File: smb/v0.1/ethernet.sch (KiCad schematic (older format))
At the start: 22 parts, among them J401 HR911105_RJ45, U201 ENC28J60, U301 74HC08, X201 25MHz

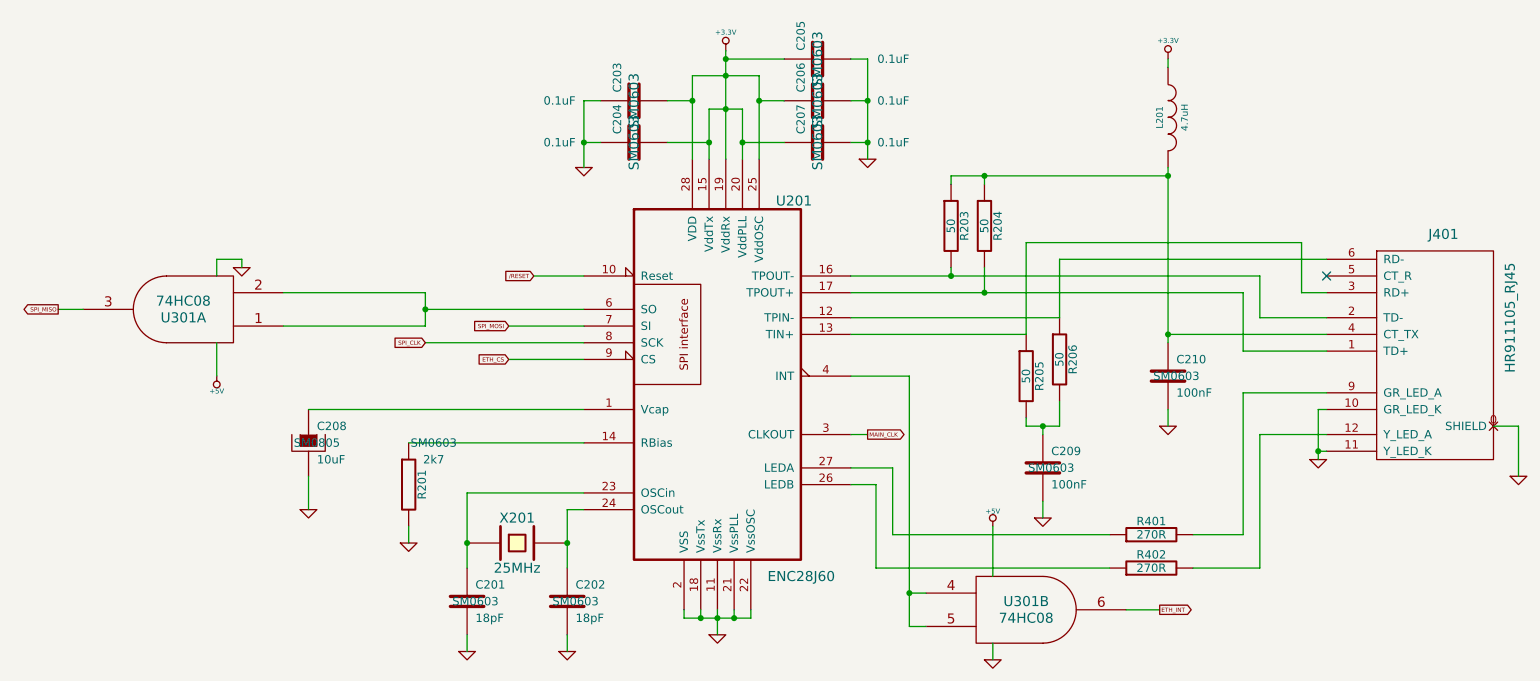
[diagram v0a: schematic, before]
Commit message: correction broche 8 du module RS485 + inversion tx+/tx- au niveau du connecteur + pilotage E/R independant inversion polarit? connecteur d'alim d?placement slot pour rtc simplification routage et optimisation plan de masse (affinage zone exclusion)
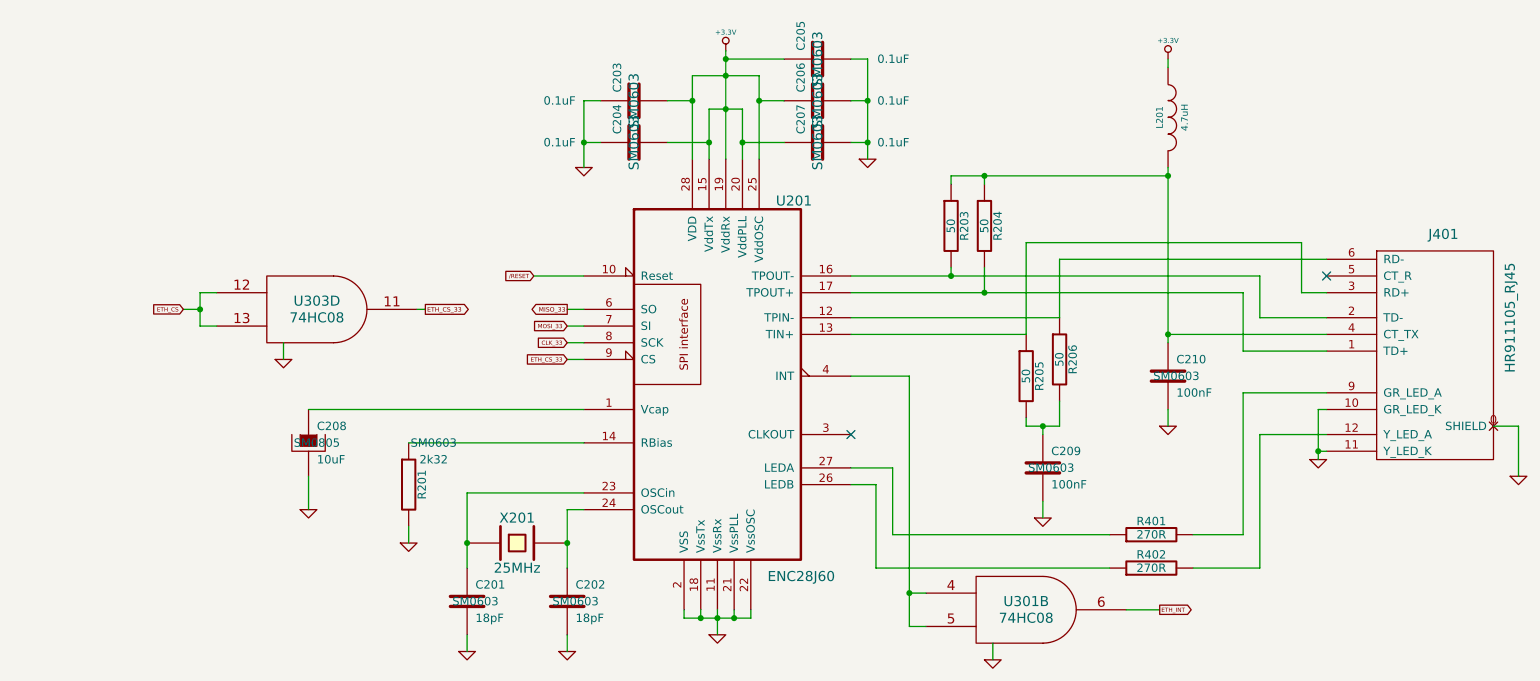
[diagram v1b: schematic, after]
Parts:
- R201: value 2k7 -> 2k32
- renumbered U301 to U303
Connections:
- net ETH_CS: now also U303.12, U303.13; no longer U201.9 (CS)
- net +5V: no longer names the net of U303.14 (VCC)
- net +5V: no longer U301.14 (VCC)
- net MAIN_CLK: no longer names the net of U201.3 (CLKOUT)
- net SPI_CLK renamed CLK_33
- removed net SPI_MISO: U303.3
- net SPI_MOSI renamed MOSI_33
- new net ETH_CS_33: U201.9 (CS), U303.11
- new net MISO_33: U201.6 (SO)
- no-connect marks 1 -> 2
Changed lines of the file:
@@
-EESchema Schematic File Version 2  date jeu. 23 mai 2013 13:21:39 CEST
+EESchema Schematic File Version 2  date mar. 28 mai 2013 22:08:00 CEST
 LIBS:power
 LIBS:device
@@
 LIBS:dual_self
 LIBS:ALPS_SWITCHS
+LIBS:max485
 LIBS:SMB-cache
-EELAYER 27 0
+EELAYER 24 0
 EELAYER END
 $Descr A4 11693 8268
@@
 Sheet 4 4
 Title "Short Main Board - SMB controler"
-Date "23 may 2013"
+Date "28 may 2013"
 Rev "0"
 Comp "XPLDUINO project"
@@
 Wire Wire Line
 	8700 4350 9000 4350
-Wire Wire Line
-	7500 5000 7500 5100
-Wire Wire Line
-	2850 3200 2850 3400
 Connection ~ 7000 4700
 Wire Wire Line
 	7100 4700 7000 4700
-Wire Wire Line
-	2050 3000 1900 3000
-Wire Wire Line
-	3250 2900 4100 2900
 Connection ~ 7450 2200
 Wire Wire Line
@@
 	4750 2800 5050 2800
 Wire Wire Line
-	6650 3750 6750 3750
-Wire Wire Line
-	4600 3100 5050 3100
-Wire Wire Line
-	4100 3200 5050 3200
-Wire Wire Line
 	4000 3800 5050 3800
 Wire Wire Line
@@
 	3400 3600 5050 3600
 Wire Wire Line
-	4100 3000 5050 3000
-Wire Wire Line
-	4600 3300 5050 3300
-Wire Wire Line
 	6650 3050 7900 3050
 Wire Wire Line
@@
 Connection ~ 8550 2200
 Wire Wire Line
-	4100 2900 4100 3100
-Wire Wire Line
-	4100 3100 3250 3100
-Connection ~ 4100 3000
-Wire Wire Line
 	6650 3400 7000 3400
 Wire Wire Line
@@
 Wire Wire Line
 	8300 4800 8500 4800
-Wire Wire Line
-	2850 2800 2850 2700
-Wire Wire Line
-	2850 2700 3000 2700
-Wire Wire Line
-	3000 2700 3000 2750
-Wire Wire Line
-	7500 4300 7500 4600
 Wire Wire Line
 	6900 4350 8200 4350
@@
 $EndComp
 $Comp
-L +5V #PWR086
-U 1 1 4FDE1BE4
-P 7500 4300
-F 0 "#PWR086" H 7500 4390 20  0001 C CNN
-F 1 "+5V" H 7500 4390 30  0000 C CNN
-F 2 "" H 7500 4300 60  0001 C CNN
-F 3 "" H 7500 4300 60  0001 C CNN
-	1    7500 4300
-	1    0    0    -1
-$EndComp
-$Comp
-L GND #PWR087
-U 1 1 4FDE1B8D
-P 7500 5100
-F 0 "#PWR087" H 7500 5100 30  0001 C CNN
-F 1 "GND" H 7500 5030 30  0001 C CNN
-F 2 "" H 7500 5100 60  0001 C CNN
-F 3 "" H 7500 5100 60  0001 C CNN
-	1    7500 5100
-	1    0    0    -1
-$EndComp
-$Comp
-L GND #PWR088
-U 1 1 4FDE1B70
-P 3000 2750
-F 0 "#PWR088" H 3000 2750 30  0001 C CNN
-F 1 "GND" H 3000 2680 30  0001 C CNN
-F 2 "" H 3000 2750 60  0001 C CNN
-F 3 "" H 3000 2750 60  0001 C CNN
-	1    3000 2750
-	1    0    0    -1
-$EndComp
-$Comp
-L +5V #PWR089
-U 1 1 4FDE1B61
-P 2850 3400
-F 0 "#PWR089" H 2850 3490 20  0001 C CNN
-F 1 "+5V" H 2850 3490 30  0000 C CNN
-F 2 "" H 2850 3400 60  0001 C CNN
-F 3 "" H 2850 3400 60  0001 C CNN
-	1    2850 3400
-	-1   0    0    1
-$EndComp
-$Comp
 L 74HC08 U301
 U 2 1 4FDE1879
@@
 $EndComp
 $Comp
-L 74HC08 U301
-U 1 1 4FDE1808
-P 2650 3000
-F 0 "U301" H 2650 3050 60  0000 C CNN
-F 1 "74HC08" H 2650 2950 60  0000 C CNN
-F 2 "" H 2650 3000 60  0001 C CNN
-F 3 "" H 2650 3000 60  0001 C CNN
-	1    2650 3000
-	-1   0    0    1
-$EndComp
-$Comp
 L R R204
 U 1 1 4FA00FEC
@@
 $EndComp
 $Comp
-L +3.3V #PWR090
+L +3.3V #PWR083
 U 1 1 4FA00F89
 P 8550 1500
-F 0 "#PWR090" H 8550 1460 30  0001 C CNN
+F 0 "#PWR083" H 8550 1460 30  0001 C CNN
 F 1 "+3.3V" H 8550 1610 30  0000 C CNN
 F 2 "" H 8550 1500 60  0001 C CNN
@@
 $EndComp
 $Comp
-L GND #PWR091
+L GND #PWR084
 U 1 1 4FA00F53
 P 8550 3700
-F 0 "#PWR091" H 8550 3700 30  0001 C CNN
+F 0 "#PWR084" H 8550 3700 30  0001 C CNN
 F 1 "GND" H 8550 3630 30  0001 C CNN
 F 2 "" H 8550 3700 60  0001 C CNN
@@
 $EndComp
 $Comp
-L GND #PWR092
+L GND #PWR085
 U 1 1 4FA00C7B
 P 9450 3900
-F 0 "#PWR092" H 9450 3900 30  0001 C CNN
+F 0 "#PWR085" H 9450 3900 30  0001 C CNN
 F 1 "GND" H 9450 3830 30  0001 C CNN
 F 2 "" H 9450 3900 60  0001 C CNN
@@
 $EndComp
 $Comp
-L GND #PWR093
+L GND #PWR086
 U 1 1 4FA00C63
 P 10650 4000
-F 0 "#PWR093" H 10650 4000 30  0001 C CNN
+F 0 "#PWR086" H 10650 4000 30  0001 C CNN
 F 1 "GND" H 10650 3930 30  0001 C CNN
 F 2 "" H 10650 4000 60  0001 C CNN
@@
 $EndComp
 $Comp
-L GND #PWR094
+L GND #PWR087
 U 1 1 4F9FF676
 P 7800 4250
-F 0 "#PWR094" H 7800 4250 30  0001 C CNN
+F 0 "#PWR087" H 7800 4250 30  0001 C CNN
 F 1 "GND" H 7800 4180 30  0001 C CNN
 F 2 "" H 7800 4250 60  0001 C CNN
@@
 Text GLabel 8500 4800 2    25   Output ~ 0
 ETH_INT
-Text GLabel 6750 3750 2    25   Output ~ 0
-MAIN_CLK
-Text GLabel 1900 3000 0    25   Output ~ 0
-SPI_MISO
-Text GLabel 4600 3100 0    25   Input ~ 0
-SPI_MOSI
-Text GLabel 4600 3300 0    25   Input ~ 0
-ETH_CS
-Text GLabel 4100 3200 0    25   Input ~ 0
-SPI_CLK
-$Comp
-L GND #PWR095
+Text GLabel 4950 3100 0    25   Input ~ 0
+MOSI_33
+Text GLabel 4950 3300 0    25   Input ~ 0
+ETH_CS_33
+Text GLabel 4950 3200 0    25   Input ~ 0
+CLK_33
+$Comp
+L GND #PWR088
 U 1 1 4F9FEE21
 P 3400 4200
-F 0 "#PWR095" H 3400 4200 30  0001 C CNN
+F 0 "#PWR088" H 3400 4200 30  0001 C CNN
 F 1 "GND" H 3400 4130 30  0001 C CNN
 F 2 "" H 3400 4200 60  0001 C CNN
@@
 $EndComp
 $Comp
-L GND #PWR096
+L GND #PWR089
 U 1 1 4F9FEE1E
 P 4000 4400
-F 0 "#PWR096" H 4000 4400 30  0001 C CNN
+F 0 "#PWR089" H 4000 4400 30  0001 C CNN
 F 1 "GND" H 4000 4330 30  0001 C CNN
 F 2 "" H 4000 4400 60  0001 C CNN
@@
 P 4000 4050
 F 0 "R201" V 4080 4050 50  0000 C CNN
-F 1 "2k7" H 4150 4200 50  0000 C CNN
+F 1 "2k32" H 4150 4200 50  0000 C CNN
 F 2 "SM0603" H 4150 4300 50  0000 C CNN
 F 3 "" H 4000 4050 60  0001 C CNN
@@
 $EndComp
 $Comp
-L GND #PWR097
+L GND #PWR090
 U 1 1 4F9FC462
 P 5050 2150
-F 0 "#PWR097" H 5050 2150 30  0001 C CNN
+F 0 "#PWR090" H 5050 2150 30  0001 C CNN
 F 1 "GND" H 5050 2080 30  0001 C CNN
 F 2 "" H 5050 2150 60  0001 C CNN
@@
 $EndComp
 $Comp
-L GND #PWR098
+L GND #PWR091
 U 1 1 4F9FC45C
 P 6750 2100
-F 0 "#PWR098" H 6750 2100 30  0001 C CNN
+F 0 "#PWR091" H 6750 2100 30  0001 C CNN
 F 1 "GND" H 6750 2030 30  0001 C CNN
 F 2 "" H 6750 2100 60  0001 C CNN
@@
 $EndComp
 $Comp
-L +3.3V #PWR099
+L +3.3V #PWR092
 U 1 1 4F9FC2EE
 P 5900 1450
-F 0 "#PWR099" H 5900 1410 30  0001 C CNN
+F 0 "#PWR092" H 5900 1410 30  0001 C CNN
 F 1 "+3.3V" H 5900 1560 30  0000 C CNN
 F 2 "" H 5900 1450 60  0001 C CNN
@@
 $EndComp
 $Comp
-L GND #PWR0100
+L GND #PWR093
 U 1 1 4F9D7261
 P 4350 5050
-F 0 "#PWR0100" H 4350 5050 30  0001 C CNN
+F 0 "#PWR093" H 4350 5050 30  0001 C CNN
 F 1 "GND" H 4350 4980 30  0001 C CNN
 F 2 "" H 4350 5050 60  0001 C CNN
@@
 $EndComp
 $Comp
-L GND #PWR0101
+L GND #PWR094
 U 1 1 4F9D725B
 P 4950 5050
-F 0 "#PWR0101" H 4950 5050 30  0001 C CNN
+F 0 "#PWR094" H 4950 5050 30  0001 C CNN
 F 1 "GND" H 4950 4980 30  0001 C CNN
 F 2 "" H 4950 5050 60  0001 C CNN
@@
 $EndComp
 $Comp
-L GND #PWR0102
+L GND #PWR095
 U 1 1 4F9D6E29
 P 5850 4950
-F 0 "#PWR0102" H 5850 4950 30  0001 C CNN
+F 0 "#PWR095" H 5850 4950 30  0001 C CNN
 F 1 "GND" H 5850 4880 30  0001 C CNN
 F 2 "" H 5850 4950 60  0001 C CNN
@@
 $EndComp
 NoConn ~ 9500 2800
+Text GLabel 4950 3000 0    27   Output ~ 0
+MISO_33
+Wire Wire Line
+	4950 3000 5050 3000
+Wire Wire Line
+	4950 3100 5050 3100
+Wire Wire Line
+	4950 3200 5050 3200
+Wire Wire Line
+	4950 3300 5050 3300
+Text GLabel 4100 3000 2    27   Output ~ 0
+ETH_CS_33
+Wire Wire Line
+	4050 3000 4100 3000
+Text GLabel 2650 3000 0    25   Input ~ 0
+ETH_CS
+Wire Wire Line
+	2650 3000 2750 3000
+Wire Wire Line
+	2750 2900 2750 3100
+Wire Wire Line
+	2750 2900 2850 2900
+Wire Wire Line
+	2750 3100 2850 3100
+Connection ~ 2750 3000
+$Comp
+L 74HC08 U303
+U 4 1 4FDE1808
+P 3450 3000
+F 0 "U303" H 3450 3050 60  0000 C CNN
+F 1 "74HC08" H 3450 2950 60  0000 C CNN
+F 2 "" H 3450 3000 60  0001 C CNN
+F 3 "" H 3450 3000 60  0001 C CNN
+	4    3450 3000
+	1    0    0    -1
+$EndComp
+NoConn ~ 6650 3750
+$Comp
+L GND #PWR096
+U 1 1 519F2E94
+P 3250 3300
+F 0 "#PWR096" H 3250 3300 30  0001 C CNN
+F 1 "GND" H 3250 3230 30  0001 C CNN
+F 2 "" H 3250 3300 60  0001 C CNN
+F 3 "" H 3250 3300 60  0001 C CNN
+	1    3250 3300
+	1    0    0    -1
+$EndComp
+Wire Wire Line
+	3250 3300 3250 3200
+$Comp
+L GND #PWR097
+U 1 1 519F367A
+P 7500 5100
+F 0 "#PWR097" H 7500 5100 30  0001 C CNN
+F 1 "GND" H 7500 5030 30  0001 C CNN
+F 2 "" H 7500 5100 60  0001 C CNN
+F 3 "" H 7500 5100 60  0001 C CNN
+	1    7500 5100
+	1    0    0    -1
+$EndComp
+Wire Wire Line
+	7500 5100 7500 5000
 $EndSCHEMATC
